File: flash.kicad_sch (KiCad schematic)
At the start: 11 parts, among them U1 LFE5U-25F-6BG381C, U10 IS25LP128F-JBLE

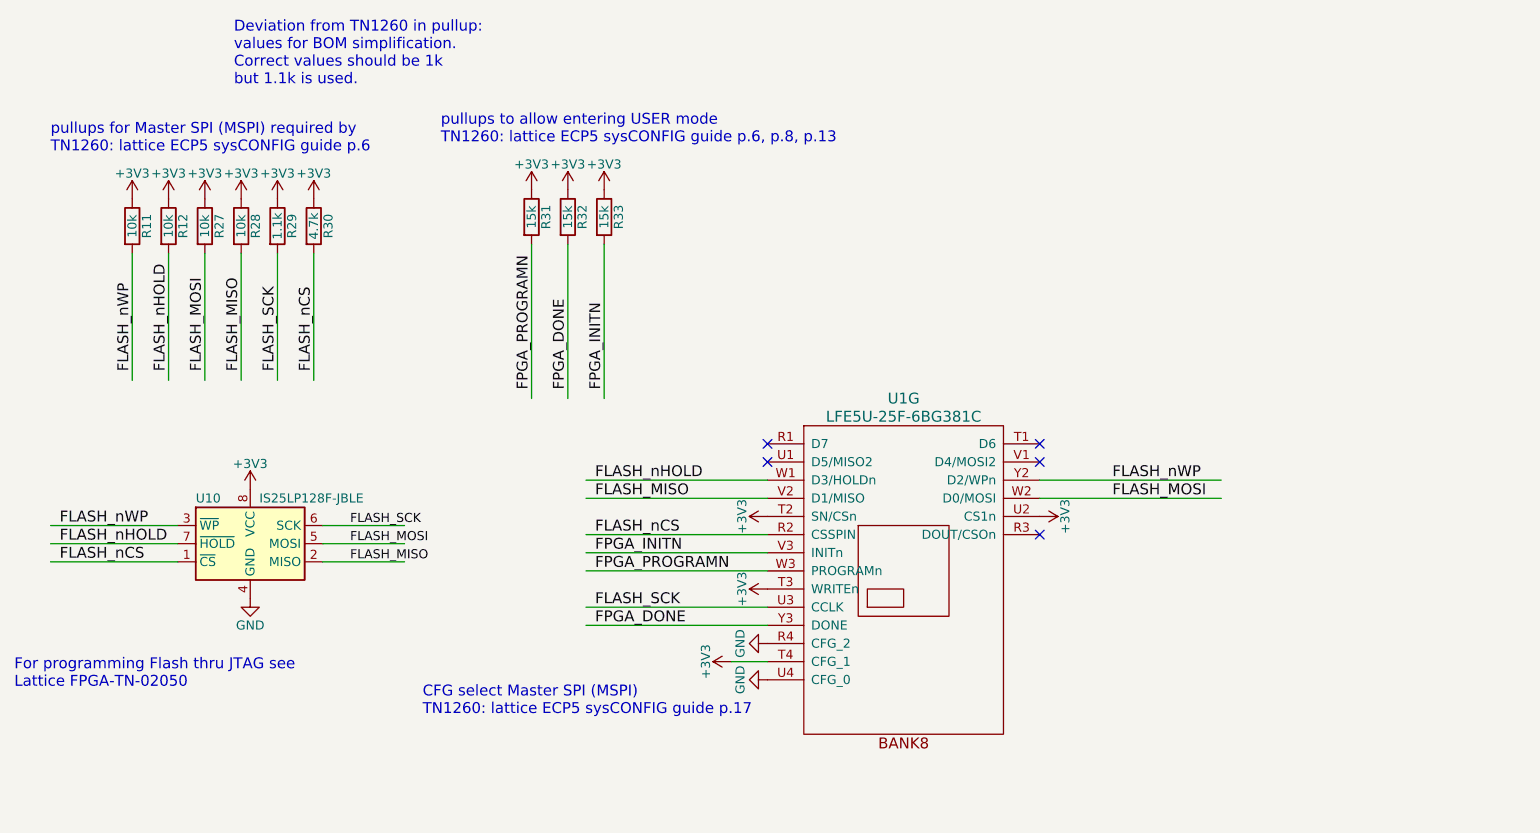
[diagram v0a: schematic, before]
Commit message: Routed Level Shifters + Flash
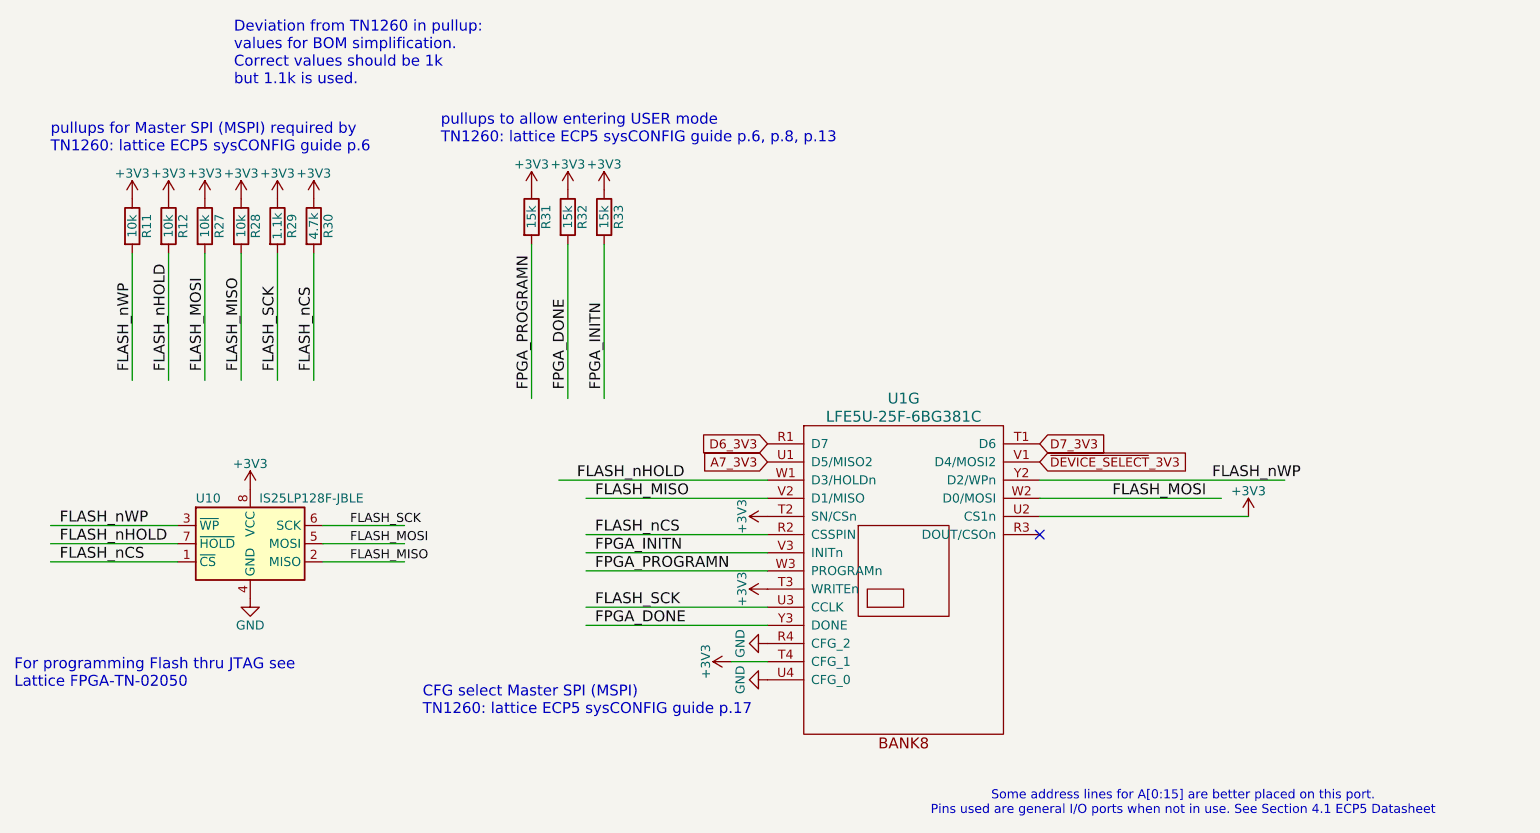
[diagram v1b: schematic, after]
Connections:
- net D6_3V3: now reaches U1.R1 (D7)
- net D7_3V3: now reaches U1.T1 (D6)
- net A7_3V3: now reaches U1.U1 (D5/MISO2)
- net ~{DEVICE_SELECT}_3V3: now reaches U1.V1 (D4/MOSI2)
- no-connect marks 5 -> 1
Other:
- note added: "Some address lines for A[0:15] are better placed on this port. Pins used are general I/O ports when not in use. See Section 4.1 ECP5 Datasheet"
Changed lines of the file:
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@@
+		)
+	)
+	(text "Some address lines for A[0:15] are better placed on this port. \nPins used are general I/O ports when not in use. See Section 4.1 ECP5 Datasheet"
+		(exclude_from_sim no)
+		(at 241.046 145.542 0)
+		(effects
+			(font
+				(size 1.27 1.27)
+			)
 		)
 	)
@@
 			(justify left bottom)
 		)
-	)
-	(no_connect
-		(at 182.88 95.25)
-	)
-	(no_connect
-		(at 182.88 97.79)
 	)
 	(no_connect
 		(at 220.98 107.95)
 	)
-	(no_connect
-		(at 220.98 95.25)
-	)
-	(no_connect
-		(at 220.98 97.79)
-	)
 	(wire
 		(pts
@@
 	(wire
 		(pts
+			(xy 153.67 100.33) (xy 182.88 100.33)
+		)
+		(stroke
+			(width 0)
+			(type default)
+		)
+	)
+	(wire
+		(pts
+			(xy 220.98 105.41) (xy 250.19 105.41)
+		)
+		(stroke
+			(width 0)
+			(type default)
+		)
+	)
+	(wire
+		(pts
 			(xy 109.22 68.58) (xy 109.22 86.36)
 		)
@@
 	(wire
 		(pts
-			(xy 182.88 100.33) (xy 157.48 100.33)
-		)
-		(stroke
-			(width 0)
-			(type default)
-		)
-	)
-	(wire
-		(pts
 			(xy 120.65 106.68) (xy 132.08 106.68)
 		)
@@
 	(wire
 		(pts
-			(xy 220.98 100.33) (xy 246.38 100.33)
+			(xy 220.98 100.33) (xy 255.27 100.33)
 		)
 		(stroke
@@
 	)
 	(label "FLASH_nHOLD"
-		(at 158.75 100.33 0)
+		(at 156.21 100.33 0)
 		(effects
 			(font
@@
 	)
 	(label "FLASH_nWP"
-		(at 231.14 100.33 0)
+		(at 245.11 100.33 0)
 		(effects
 			(font
@@
 		)
 	)
+	(global_label "D7_3V3"
+		(shape input)
+		(at 220.98 95.25 0)
+		(effects
+			(font
+				(size 1.27 1.27)
+			)
+			(justify left)
+		)
+		(property "Intersheetrefs" "${INTERSHEET_REFS}"
+			(at 220.98 95.25 90)
+			(effects
+				(font
+					(size 1.27 1.27)
+				)
+				(hide yes)
+			)
+		)
+	)
+	(global_label "A7_3V3"
+		(shape input)
+		(at 182.88 97.79 180)
+		(effects
+			(font
+				(size 1.27 1.27)
+			)
+			(justify right)
+		)
+		(property "Intersheetrefs" "${INTERSHEET_REFS}"
+			(at 182.88 97.79 90)
+			(effects
+				(font
+					(size 1.27 1.27)
+				)
+				(hide yes)
+			)
+		)
+	)
+	(global_label "~{DEVICE_SELECT}_3V3"
+		(shape input)
+		(at 220.98 97.79 0)
+		(effects
+			(font
+				(size 1.27 1.27)
+			)
+			(justify left)
+		)
+		(property "Intersheetrefs" "${INTERSHEET_REFS}"
+			(at 220.98 97.79 90)
+			(effects
+				(font
+					(size 1.27 1.27)
+				)
+				(hide yes)
+			)
+		)
+	)
+	(global_label "D6_3V3"
+		(shape input)
+		(at 182.88 95.25 180)
+		(effects
+			(font
+				(size 1.27 1.27)
+			)
+			(justify right)
+		)
+		(property "Intersheetrefs" "${INTERSHEET_REFS}"
+			(at 182.88 95.25 90)
+			(effects
+				(font
+					(size 1.27 1.27)
+				)
+				(hide yes)
+			)
+		)
+	)
 	(symbol
 		(lib_id "Memory_EEPROM:25LCxxx")
@@
 	(symbol
 		(lib_id "power:+3V3")
-		(at 220.98 105.41 270)
+		(at 250.19 105.41 0)
+		(mirror y)
 		(unit 1)
 		(exclude_from_sim no)
@@
 		(dnp no)
 		(property "Reference" "#PWR0167"
-			(at 217.17 105.41 0)
+			(at 250.19 109.22 0)
 			(effects
 				(font
@@
 		)
 		(property "Value" "+3V3"
-			(at 224.536 105.41 0)
+			(at 250.19 101.854 0)
 			(effects
 				(font
@@
 		)
 		(property "Footprint" ""
-			(at 220.98 105.41 0)
-			(effects
-				(font
-					(size 1.27 1.27)
-				)
-			)
-		)
-		(property "Datasheet" ""
-			(at 220.98 105.41 0)
-			(effects
-				(font
-					(size 1.27 1.27)
-				)
-			)
-		)
-		(property "Description" ""
-			(at 220.98 105.41 0)
-			(effects
-				(font
+			(at 250.19 105.41 0)
+			(effects
+				(font
+					(size 1.27 1.27)
+				)
+			)
+		)
+		(property "Datasheet" ""
+			(at 250.19 105.41 0)
+			(effects
+				(font
+					(size 1.27 1.27)
+				)
+			)
+		)
+		(property "Description" ""
+			(at 250.19 105.41 0)
+			(effects
+				(font
